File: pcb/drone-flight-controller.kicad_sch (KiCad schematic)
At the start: 77 parts, among them J1 SWD, J10 CONN_MANDO, J11 OLED, J12 STM32 SPI, J13 STM32 I2C, J14 STM32 USART, J2 Jumper, J3 USB_B_Micro, J4 CONN_MOT_1, J5 CONN_MOT_2, J6 CONN_MOT_3, J7 CONN_MOT_4, J8 XT-60, J9 LIDAR, SW1 RST, SW2 BOTON, U1 STM32F103R8T6, U2 MPU-6050, Y1 8MHz, Y2 32.768KHz

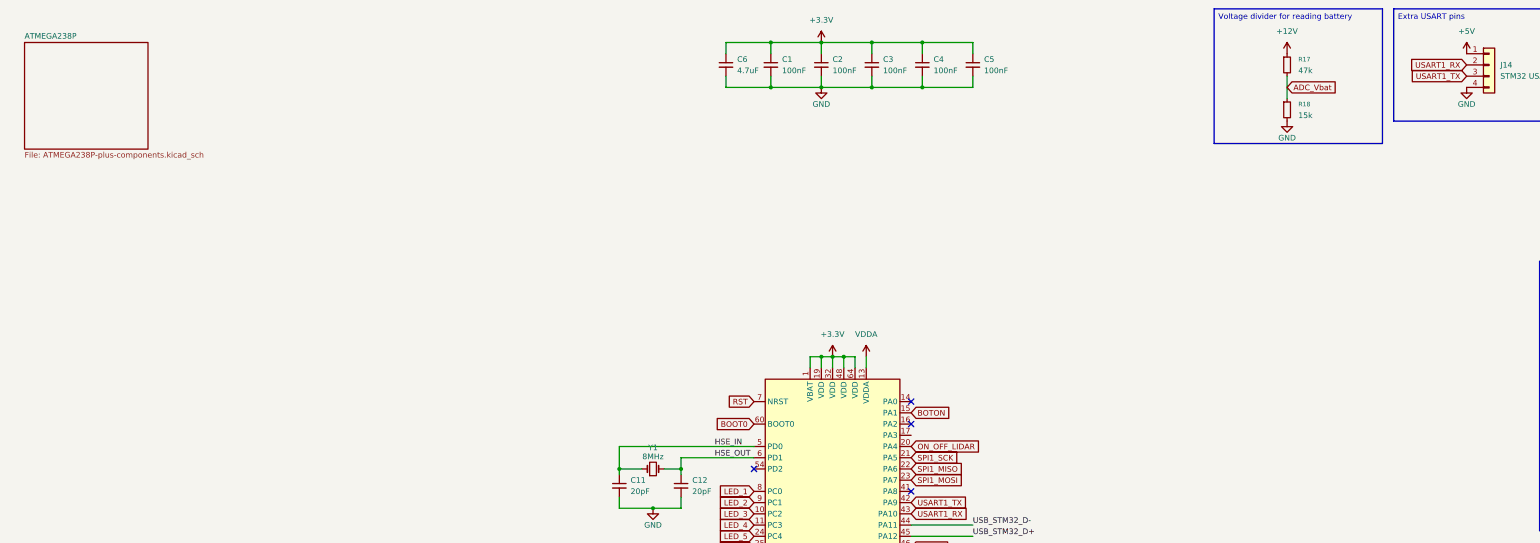
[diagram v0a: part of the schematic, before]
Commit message: added sd card, RF module and power supply
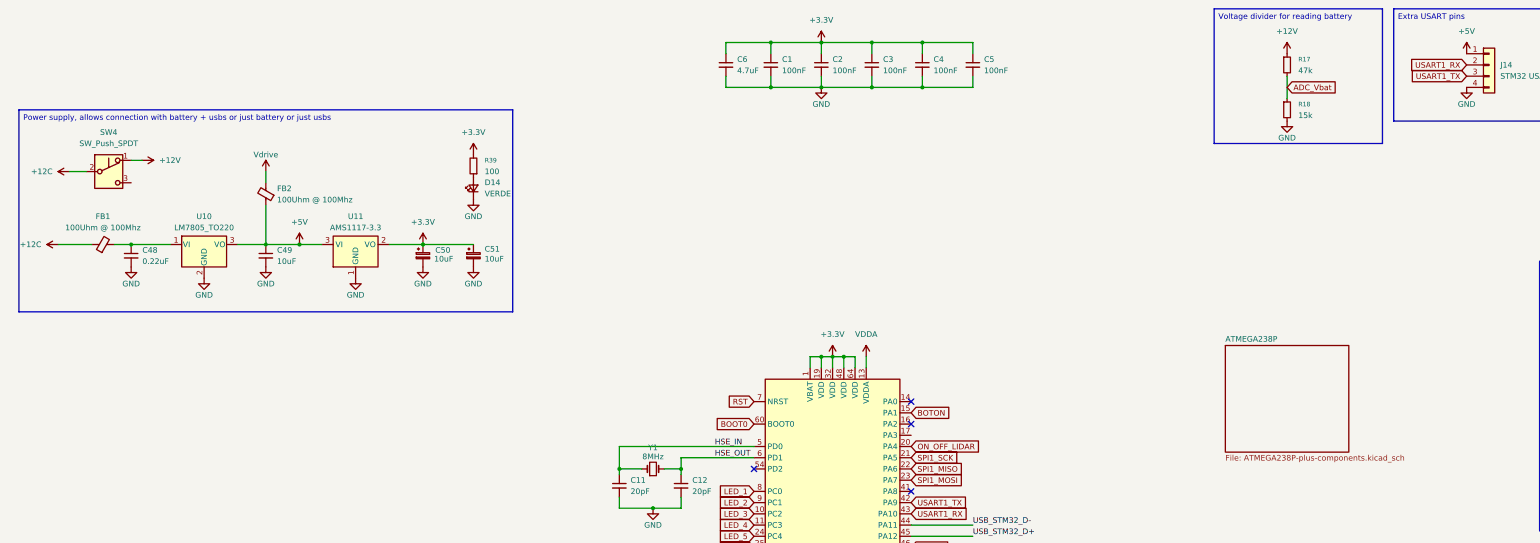
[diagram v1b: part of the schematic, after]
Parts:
- added C48: 0.22uF, symbol Device:C_Small
- added C49: 10uF, symbol Device:C_Small
- added C50, C51: 10uF, symbol Device:C_Polarized_Small
- added D14: VERDE, symbol Device:LED_Small
- added FB1, FB2: 100Uhm @ 100Mhz, symbol Device:FerriteBead_Small
- added R39: 100, symbol Device:R_Small
- added SW4: SW_Push_SPDT, symbol Switch:SW_Push_SPDT
- added U10: LM7805_TO220, Package_TO_SOT_THT:TO-220-3_Vertical, symbol Regulator_Linear:LM7805_TO220
- added U11: AMS1117-3.3, Package_TO_SOT_SMD:SOT-223-3_TabPin2, symbol Regulator_Linear:AMS1117-3.3
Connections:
- net +12V: now also SW4.1 (A)
- net +3.3V: now also C50.1, C51.1, R39.2, U11.2 (VO)
- net +5V: now also C49.1, FB2.1, U10.3 (VO), U11.3 (VI)
- net GND: now also C48.2, C49.2, C50.2, C51.2, D14.1 (K), U10.2 (GND), U11.1 (GND)
- net Vdrive: now also FB2.2
- new net: D14.2 (A), R39.1
- new net: C48.1, FB1.2, U10.1 (VI)
- new net +12C: FB1.1, SW4.2 (B)

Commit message: pcb: source the tact switches as SHOU HAN TS24CA (C393942)
Give SW1 (STM32 reset), SW2 (user button), and SW3 (ATmega reset) a real
orderable part: footprint, LCSC/MPN fields, and datasheet, so they stop
blocking BOM/footprint coverage. One part number covers all three buttons;
side actuation keeps them reachable from the board edge. SW4 is deliberately
untouched — it is the master power switch and needs a latching, adequately
rated part, tracked in DESIGN_REVIEW and the new parts log.
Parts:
- SW1: value RST -> TS24CA_C393942; footprint (none) -> easyeda:SW-SMD_2P-TS24CA; LCSC (none) -> C393942; Manufacturer (none) -> SHOU HAN; Part (none) -> TS24CA
- SW2: value BOTON -> TS24CA_C393942; footprint (none) -> easyeda:SW-SMD_2P-TS24CA; LCSC (none) -> C393942; Manufacturer (none) -> SHOU HAN; Part (none) -> TS24CA
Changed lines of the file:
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@@
 			)
 		)
-		(property "Value" "BOTON"
+		(property "Value" "TS24CA_C393942"
 			(at 385.064 162.56 90)
 			(show_name no)
@@
 			)
 		)
-		(property "Footprint" ""
+		(property "Footprint" "easyeda:SW-SMD_2P-TS24CA"
 			(at 387.35 161.29 0)
 			(hide yes)
@@
 			)
 		)
-		(property "Datasheet" ""
+		(property "Datasheet" "https://www.lcsc.com/datasheet/lcsc_datasheet_2404241539_SHOU-HAN-TS24CA_C393942.pdf"
 			(at 387.35 161.29 0)
 			(hide yes)
@@
 			)
 		)
-		(property "Description" "Push button switch, generic, two pins"
+		(property "Description" "-20℃~+70℃ 1.6N 1.9mm 12V 20,000 cycles 3.5mm 4.7mm 50mA Black No Rectangular Button SMD(SMT) Tab SPST Surface Mount, Right Angle Without Bracket SMD,4.6x1.8mm Tactile Switches ROHS"
 			(at 382.27 161.29 0)
 			(hide yes)
@@
 			)
 		)
+    (property "LCSC" "C393942" (at 382.27 161.29 0)
+      (effects (font (size 1.27 1.27)) (hide yes))
+    )
+    (property "Part" "TS24CA" (at 382.27 161.29 0)
+      (effects (font (size 1.27 1.27)) (hide yes))
+    )
+    (property "Manufacturer" "SHOU HAN" (at 382.27 161.29 0)
+      (effects (font (size 1.27 1.27)) (hide yes))
+    )
 		(pin "2"
 		)
@@
 			)
 		)
-		(property "Value" "RST"
+		(property "Value" "TS24CA_C393942"
 			(at 25.4 199.3899 90)
 			(show_name no)
@@
 			)
 		)
-		(property "Footprint" ""
+		(property "Footprint" "easyeda:SW-SMD_2P-TS24CA"
 			(at 26.67 198.12 0)
 			(hide yes)
@@
 			)
 		)
-		(property "Datasheet" ""
+		(property "Datasheet" "https://www.lcsc.com/datasheet/lcsc_datasheet_2404241539_SHOU-HAN-TS24CA_C393942.pdf"
 			(at 26.67 198.12 0)
 			(hide yes)
@@
 			)
 		)
-		(property "Description" "Push button switch, generic, two pins"
+		(property "Description" "-20℃~+70℃ 1.6N 1.9mm 12V 20,000 cycles 3.5mm 4.7mm 50mA Black No Rectangular Button SMD(SMT) Tab SPST Surface Mount, Right Angle Without Bracket SMD,4.6x1.8mm Tactile Switches ROHS"
 			(at 21.59 198.12 0)
 			(hide yes)
@@
 			)
 		)
+    (property "LCSC" "C393942" (at 21.59 198.12 0)
+      (effects (font (size 1.27 1.27)) (hide yes))
+    )
+    (property "Part" "TS24CA" (at 21.59 198.12 0)
+      (effects (font (size 1.27 1.27)) (hide yes))
+    )
+    (property "Manufacturer" "SHOU HAN" (at 21.59 198.12 0)
+      (effects (font (size 1.27 1.27)) (hide yes))
+    )
 		(pin "2"
 		)

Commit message: footprint assignments
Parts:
- C1, C10, C11, C12, C13, C14, C15, C16, C17, C18, C19, C2, C3, C4, C5, C6, C7, C8, C9: footprint (none) -> Capacitor_SMD:C_0402_1005Metric
- C48, C49, C50, C51: footprint (none) -> Capacitor_SMD:C_1206_3216Metric
- D1, D2: footprint (none) -> Diode_SMD:D_SOD-123
- D14, D4, D5, D6, D7, D8, D9: footprint (none) -> LED_SMD:LED_0603_1608Metric
- FB1, FB2: footprint (none) -> Inductor_SMD:L_0805_2012Metric
- H1, H2, H3, H4, H5, H6, H7, H8: footprint (none) -> easyeda:MountingHole_3.5mm_5.5mm
- J1, J13: footprint (none) -> Connector_PinHeader_2.54mm:PinHeader_1x04_P2.54mm_Vertical
- J10: footprint (none) -> Connector_PinHeader_2.54mm:PinHeader_2x04_P2.54mm_Vertical
- J11: footprint (none) -> easyeda:OLED
- J12: footprint (none) -> Connector_PinHeader_2.54mm:PinHeader_1x06_P2.54mm_Vertical
- J14: footprint (none) -> Connector_PinHeader_2.54mm:PinHeader_1x04_P2.54mm_Horizontal
- J2, J4, J5, J6, J7: footprint (none) -> Connector_PinHeader_2.54mm:PinHeader_1x03_P2.54mm_Vertical
- J3: footprint (none) -> easyeda:MICRO-USB-SMD_5P-P0.65-H-F_MICRO5.9MMUSB
- J8: footprint (none) -> easyeda:AMASS_XT60-M
- J9: footprint (none) -> Connector_PinHeader_2.54mm:PinHeader_1x06_P2.54mm_Horizontal
- L1: footprint (none) -> Inductor_SMD:L_0402_1005Metric
- R1, R10, R17, R18, R19, R2, R20, R3, R4, R5, R6, R7, R8, R9: footprint (none) -> Resistor_SMD:R_0402_1005Metric
- R11, R12, R13, R14, R15, R16, R39: footprint (none) -> Resistor_SMD:R_0603_1608Metric
- SW4: footprint (none) -> easyeda:Switch_Slide
- U10: footprint Package_TO_SOT_THT:TO-220-3_Vertical -> Package_TO_SOT_THT:TO-220-3_Horizontal_TabDown
- Y1: footprint (none) -> Crystal:Crystal_SMD_5032-2Pin_5.0x3.2mm
- Y2: footprint (none) -> Crystal:Crystal_SMD_2012-2Pin_2.0x1.2mm

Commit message: erc: first clean native run, plus full footprint assignment
Fix the CH340G VCC/V3 cross-wiring (the chip was unpowered and its
internal 3.3 V node sat on the 5 V rail), add PWR_FLAGs to the
passive-fed rails and GND, no-connect SW4's unused throw, and retype
the USB shell grounds to passive - ERC now reports 0/0 on both sheets.
Assign footprints to every remaining component and import all 158 into
the board so layout can start. Two known netlist gaps recorded in
DESIGN_REVIEW: the USB shield pads (symbol SH vs footprint 6) and the
nRF24 exposed pad are floating; MPN coverage is still four parts.
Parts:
- U10: footprint Package_TO_SOT_THT:TO-220-3_Horizontal_TabDown -> Package_TO_SOT_THT:TO-220-3_Vertical
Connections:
- no-connect marks 20 -> 22
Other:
- moved on the sheet: J8

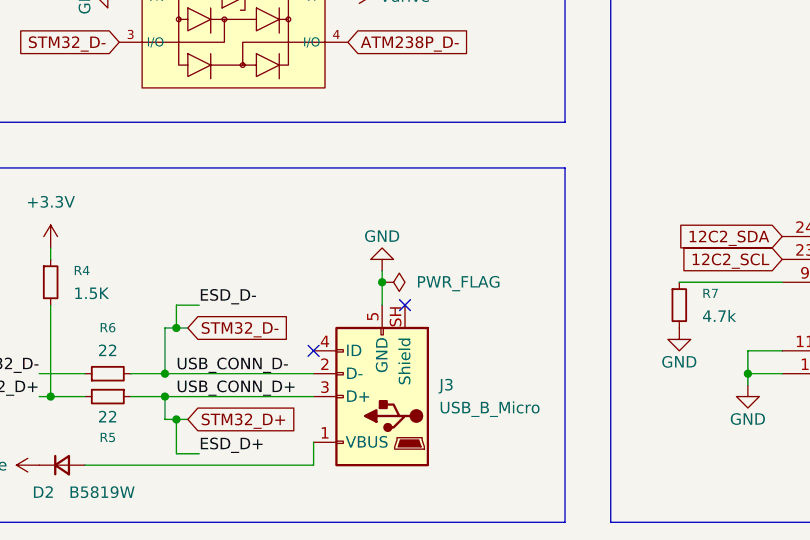
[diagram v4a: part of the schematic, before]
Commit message: pcb: ground the USB shields; leave the nRF24 EP per datasheet
The Update-PCB import exposed that J3/J16's shield pin was numbered SH
while the footprint's shell pads are numbered 6, and the pin was not
wired to anything - both connector shells would have floated. Renumber
the pin to 6 (KiCad's own USB symbol convention) and tie it to GND.
U7's exposed pad is deliberately left unconnected: the nRF24L01+
Product Specification v1.0 (p. 65) recommends keeping the die attach
pad unconnected, so the pad-21 import warning is expected.
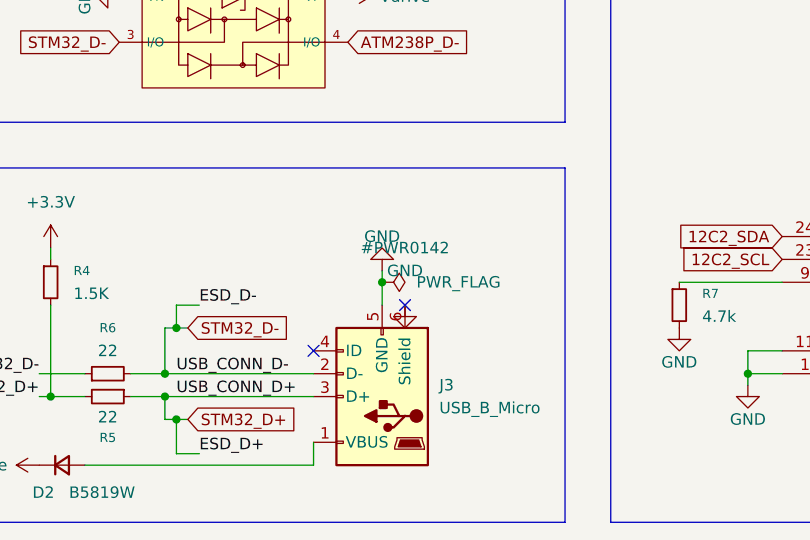
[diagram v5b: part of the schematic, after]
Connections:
- net GND: now also J3.6 (Shield)
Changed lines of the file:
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@@
 		(pin "1"
 		)
-		(pin "SH"
+		(pin "6"
 		)
 		(pin "4"
@@
 		)
 	)
-	(sheet_instances
+	  (symbol (lib_id "power:GND") (at 113.03 259.08 0) (unit 1)
+    (in_bom yes) (on_board yes) (dnp no)
+    (property "Reference" "#PWR0142" (at 113.03 252.73 0.0)
+      (effects
+    				(font
+    					(size 1.27 1.27)
+    				)
+    			)
+    )
+    (property "Value" "GND" (at 113.03 255.27 0.0)
+      (effects
+    				(font
+    					(size 1.27 1.27)
+    				)
+    			)
+    )
+    (property "Footprint" "" (at 113.03 259.08 0)
+      (effects (font (size 1.27 1.27)) (hide yes))
+    )
+    (property "Datasheet" "~" (at 113.03 259.08 0)
+      (effects (font (size 1.27 1.27)) (hide yes))
+    )
+    (instances
+      (project "project"
+        (path "/"
+          (reference "#PWR0142")
+          (unit 1)
+        )
+      )
+    )
+  )
+  (sheet_instances
 		(path "/"
 			(page "1")
